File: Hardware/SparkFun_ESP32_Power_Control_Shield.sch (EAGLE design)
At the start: 66 parts, among them IC1 OP-AMP, IC2 OP-AMP, J1 5.5x2.1mm Barrel, U1 MC33926, U2 MC33926, U3 MC33926, U4 LM317

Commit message: Added measurements for board size and version number
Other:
- note added: "VCC : 5-28VDC"
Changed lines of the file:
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@@
 GND - SLOW - 3 us
 3.3V - FAST - 1.45 us</text>
+<text x="149.86" y="157.48" size="1.778" layer="97">VCC : 5-28VDC</text>
+<text x="172.72" y="81.28" size="1.778" layer="97">VCC : 5-28VDC</text>
 </plain>
 <instances>

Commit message: Added external capacitor
External capacitor will be populated by end user if too much ripple is
present on power rail.
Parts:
- added C19: Ext., SparkFun-Capacitors:100UF-POLAR-RADIAL-2.5MM-25V-20%
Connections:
- net GND: now also C19.-
- net VCC: now also C19.+
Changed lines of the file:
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@@
 <part name="GND26" library="SparkFun-PowerSymbols" deviceset="GND" device=""/>
 <part name="GND29" library="SparkFun-PowerSymbols" deviceset="GND" device=""/>
+<part name="C19" library="SparkFun-Capacitors" deviceset="100UF-POLAR" device="-RADIAL-2.5MM-25V-20%" value="Ext."/>
 </parts>
 <sheets>
@@
 <instance part="GND26" gate="1" x="203.2" y="40.64"/>
 <instance part="GND29" gate="1" x="233.68" y="40.64"/>
+<instance part="C19" gate="G$1" x="180.34" y="162.56" rot="MR0"/>
 </instances>
 <busses>
@@
 <wire x1="198.12" y1="172.72" x2="193.04" y2="172.72" width="0.1524" layer="91"/>
 <wire x1="193.04" y1="172.72" x2="187.96" y2="172.72" width="0.1524" layer="91"/>
-<wire x1="187.96" y1="172.72" x2="167.64" y2="172.72" width="0.1524" layer="91"/>
+<wire x1="187.96" y1="172.72" x2="180.34" y2="172.72" width="0.1524" layer="91"/>
+<wire x1="180.34" y1="172.72" x2="167.64" y2="172.72" width="0.1524" layer="91"/>
 <wire x1="198.12" y1="165.1" x2="198.12" y2="172.72" width="0.1524" layer="91"/>
 <junction x="198.12" y="172.72"/>
@@
 <wire x1="193.04" y1="175.26" x2="193.04" y2="172.72" width="0.1524" layer="91"/>
 <junction x="193.04" y="172.72"/>
+<pinref part="C19" gate="G$1" pin="+"/>
+<wire x1="180.34" y1="165.1" x2="180.34" y2="172.72" width="0.1524" layer="91"/>
+<junction x="180.34" y="172.72"/>
 </segment>
 <segment>
@@
 <wire x1="170.18" y1="167.64" x2="170.18" y2="142.24" width="0.1524" layer="91"/>
 <junction x="170.18" y="167.64"/>
-<wire x1="187.96" y1="142.24" x2="170.18" y2="142.24" width="0.1524" layer="91"/>
+<wire x1="187.96" y1="142.24" x2="180.34" y2="142.24" width="0.1524" layer="91"/>
 <pinref part="C15" gate="G$1" pin="2"/>
+<wire x1="180.34" y1="142.24" x2="170.18" y2="142.24" width="0.1524" layer="91"/>
 <wire x1="187.96" y1="142.24" x2="187.96" y2="157.48" width="0.1524" layer="91"/>
 <pinref part="C16" gate="G$1" pin="2"/>
@@
 <wire x1="238.76" y1="142.24" x2="228.6" y2="142.24" width="0.1524" layer="91"/>
 <junction x="228.6" y="142.24"/>
-</segment>
-<segment>
+<pinref part="C19" gate="G$1" pin="-"/>
+<wire x1="180.34" y1="157.48" x2="180.34" y2="142.24" width="0.1524" layer="91"/>
+<junction x="180.34" y="142.24"/>
+</segment>
+<segment>

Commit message: Proto design review changes
- Replaced SMD barrel jack with PTH
- Replaced op-amp resistor with 15k resistor
- Moved IO away from pins 34-39
- Attached disable input pin to IO pin
- Replaced 3/4 2-pin screw terminals with 6-pin screw terminal
- Added labeling to all IO pins used
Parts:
- C15: value 10uF -> Ext.; device SparkFun-Capacitors:10UF-1210-50V-20% -> SparkFun-Capacitors:100UF-POLAR-RADIAL-2.5MM-25V-20%
- C16, C18: value 0.1uF -> 10uF; device SparkFun-Capacitors:0.1UF-0603-100V-10% -> SparkFun-Capacitors:10UF-1210-50V-20%
- C17: value 10uF -> 0.1uF; device SparkFun-Capacitors:10UF-1210-50V-20% -> SparkFun-Capacitors:0.1UF-0603-100V-10%
- C19: value Ext. -> 0.1uF; device SparkFun-Capacitors:100UF-POLAR-RADIAL-2.5MM-25V-20% -> SparkFun-Capacitors:0.1UF-0603-100V-10%
- R11: value 390 -> 15k; device SparkFun-Resistors:390OHM-0603-1/10W-1% -> SparkFun-Resistors:15KOHM-0603-1/10W-1%
- U1, U2, U3: device Power_Control_Adapter_Temp:MC33926 -> SparkFun_ESP32_Power_Control_Shield_Temp:MC33926
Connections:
- net 3.3V: now also IC1G3.P$V+, IC2G3.P$V+; no longer IC1A.V+, IC2A.V+
- net 5V: now also C19.1; no longer C17.1
- net FB2: now also IC1G2.OUT; no longer IC1B.OUT
- net FB4: now also IC1G1.OUT; no longer IC1A.OUT
- net FB6: now also IC2G1.OUT; no longer IC2A.OUT
- net GND: now also C15.-, C19.2, IC1G3.P$V-, IC2G3.P$V-; no longer C15.2, C19.-, IC1A.V-, IC2A.V-
- net I_SENSE1: now also IC1G2.+IN; no longer IC1B.+IN
- net I_SENSE2: now also IC1G1.+IN; no longer IC1A.+IN
- net I_SENSE3: now also IC2G1.+IN; no longer IC2A.+IN
- net N$2: now also IC1G2.-IN; no longer IC1B.-IN
- net N$4: now also IC2G1.-IN; no longer IC2A.-IN
- net N$5: now also IC1G1.-IN; no longer IC1A.-IN
- net VCC: now also C15.+, C17.1; no longer C15.1, C19.+
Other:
- moved on the sheet: C10, C11, C12, C13, C14, C16, C17, C18, R10, R11, R12, R4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

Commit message: Same changes as design review
Forgot to save changes before commit.
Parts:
- removed J3, J4, J5: (no value), SparkFun-Connectors:CONN_023.5MM_LOCK
- added J6: (no value), SparkFun-Connectors:CONN_063.5MM-6
- J1: value 5.5x2.1mm Barrel -> POWER_JACKPTH_LOCK; device SparkFun-Connectors:POWER_JACKSMD -> SparkFun-Connectors:POWER_JACKPTH_LOCK
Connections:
- new net D1: B1.5, U1.D1, U2.D1, U3.D1
- net CTRL_2: now also B1.18; no longer B1.35
- net CTRL_3: now also B1.23; no longer B1.34
- net CTRL_6: now also B1.19; no longer B1.39
- net GND: no longer U1.D1, U2.D1, U3.D1
- net P_OUT1: now also J6.6; no longer J3.2
- net P_OUT2: now also J6.5; no longer J3.1
- net P_OUT3: now also J6.4; no longer J4.2
- net P_OUT4: now also J6.3; no longer J4.1
- net P_OUT5: now also J6.2; no longer J5.2
- net P_OUT6: now also J6.1; no longer J5.1

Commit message: QC Fixes
Replaced 0.1uF capacitors CAP-00810 with CAP-08390
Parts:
- C13, C14: device SparkFun-Capacitors:0.1UF-0603-25V-(+80/-20%) -> SparkFun-Capacitors:0.1UF-0603-100V-10%
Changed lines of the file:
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@@
 <part name="R10" library="SparkFun-Resistors" deviceset="15KOHM" device="-0603-1/10W-1%" value="15k"/>
 <part name="GND16" library="SparkFun-PowerSymbols" deviceset="GND" device=""/>
-<part name="C13" library="SparkFun-Capacitors" deviceset="0.1UF" device="-0603-25V-(+80/-20%)" value="0.1uF"/>
+<part name="C13" library="SparkFun-Capacitors" deviceset="0.1UF" device="-0603-100V-10%" value="0.1uF"/>
 <part name="SUPPLY13" library="SparkFun-PowerSymbols" deviceset="3.3V" device=""/>
 <part name="GND19" library="SparkFun-PowerSymbols" deviceset="GND" device=""/>
@@
 <part name="R12" library="SparkFun-Resistors" deviceset="15KOHM" device="-0603-1/10W-1%" value="15k"/>
 <part name="GND12" library="SparkFun-PowerSymbols" deviceset="GND" device=""/>
-<part name="C14" library="SparkFun-Capacitors" deviceset="0.1UF" device="-0603-25V-(+80/-20%)" value="0.1uF"/>
+<part name="C14" library="SparkFun-Capacitors" deviceset="0.1UF" device="-0603-100V-10%" value="0.1uF"/>
 <part name="SUPPLY14" library="SparkFun-PowerSymbols" deviceset="3.3V" device=""/>
 <part name="GND20" library="SparkFun-PowerSymbols" deviceset="GND" device=""/>

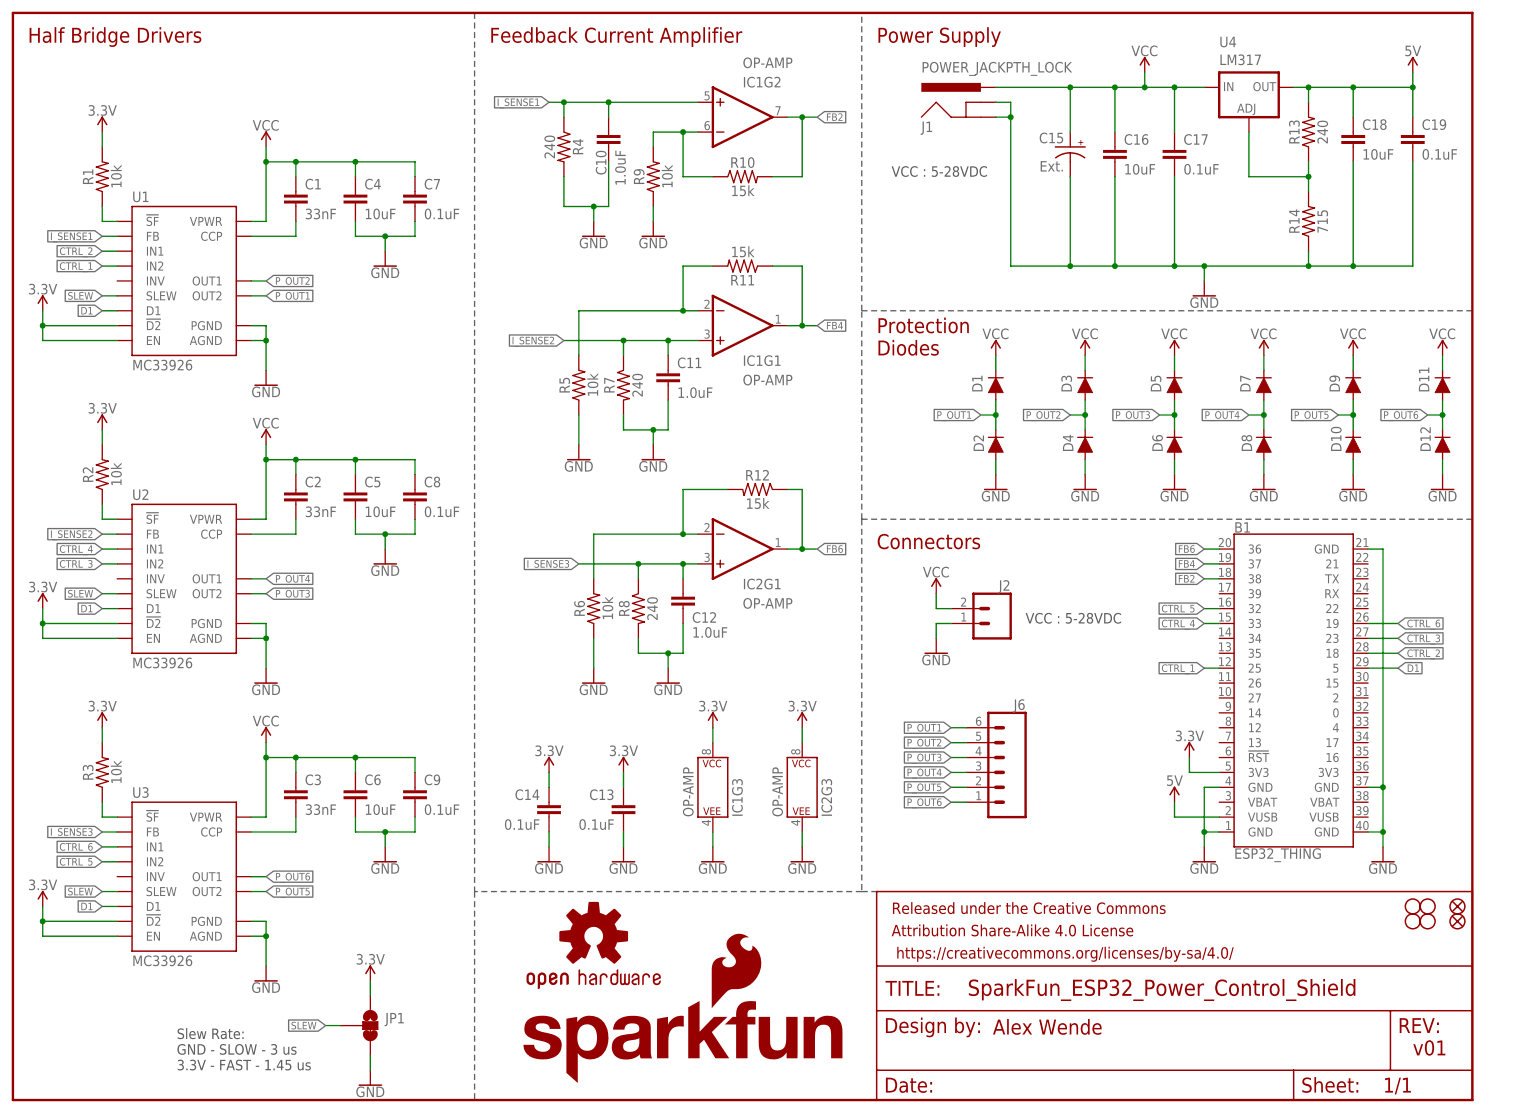
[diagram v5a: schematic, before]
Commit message: v10 Changes
- Flipped connectors from top layer to bottom
- Replaced 2-pin power connector with a 3-pin. Additional pin breaks out
5V power rail for a 5VDC fan.
- Added pull-down resistor to disable output (enabled by default).
- Replaced 5V LDO with DC/DC converter
- Replaced 240ohm resistors with 220ohm
- Replaced 15k feedback resistors with solder jumper and unpopulated PTH
resistor
- Increased trace width on VCC rail
- Added 5V bypass jumper to bypass the DC/DC converter which has a
minimum input voltage of 7V.
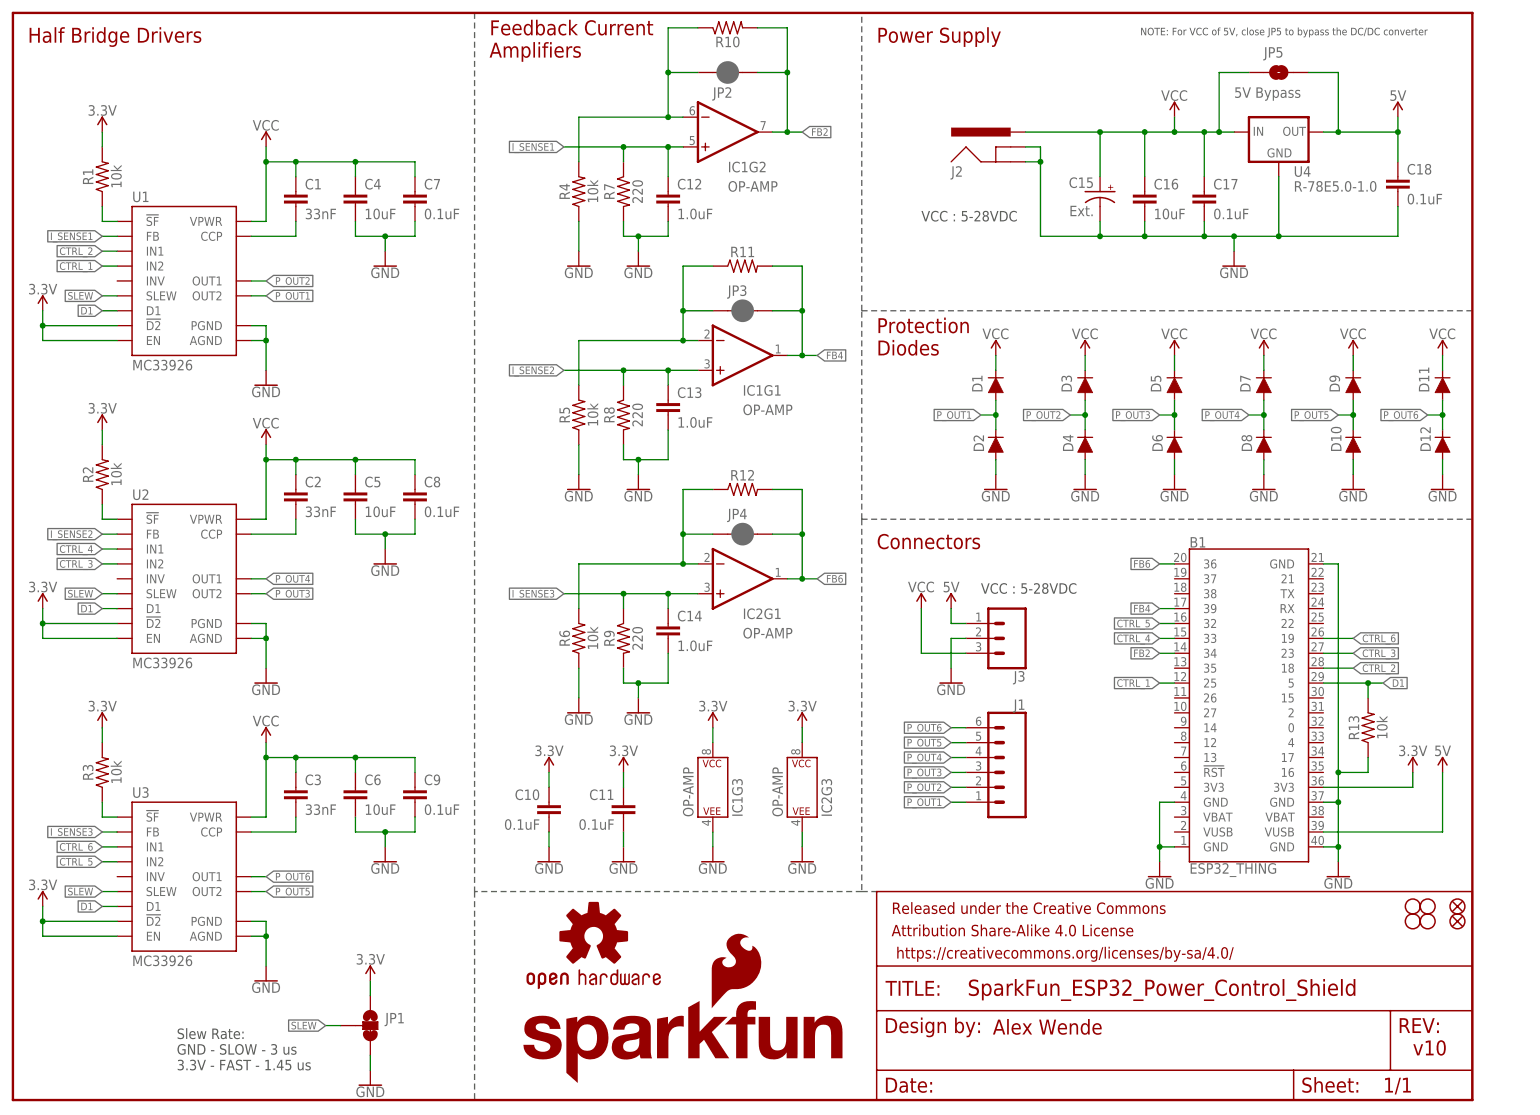
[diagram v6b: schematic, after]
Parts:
- removed C19: 0.1uF, SparkFun-Capacitors:0.1UF-0603-100V-10%
- removed J6: (no value), SparkFun-Connectors:CONN_063.5MM-6
- removed R14: 715, SparkFun-Resistors:715OHM-0603-1/10W-1%
- added J3: (no value), SparkFun-Connectors:CONN_03SCREW
- added JP2, JP3, JP4: JUMPER-SMT_2_NC_PASTE_NO-SILK, SparkFun-Jumpers:JUMPER-SMT_2_NC_PASTE_NO-SILK
- added JP5: 5V Bypass, SparkFun-Jumpers:JUMPER-SMT_2_NO_SILK
- C10, C11: value 1.0uF -> 0.1uF; device SparkFun-Capacitors:1.0UF-0603-16V-10% -> SparkFun-Capacitors:0.1UF-0603-100V-10%
- C13, C14: value 0.1uF -> 1.0uF; device SparkFun-Capacitors:0.1UF-0603-100V-10% -> SparkFun-Capacitors:1.0UF-0603-16V-10%
- C18: value 10uF -> 0.1uF; device SparkFun-Capacitors:10UF-1210-50V-20% -> SparkFun-Capacitors:0.1UF-0603-100V-10%
- J1: value POWER_JACKPTH_LOCK -> (none); device SparkFun-Connectors:POWER_JACKPTH_LOCK -> SparkFun-Connectors:CONN_063.5MM-6
- J2: value (none) -> POWER_JACKPTH_LOCK; device SparkFun-Connectors:CONN_023.5MM_LOCK -> SparkFun-Connectors:POWER_JACKPTH_LOCK
- R10, R11, R12: value 15k -> 1KOHM-HORIZ-1/4W-1%; device SparkFun-Resistors:15KOHM-0603-1/10W-1% -> SparkFun-Resistors:1KOHM-HORIZ-1/4W-1%
- R13, R4: value 240 -> 10k; device SparkFun-Resistors:240OHM-0603-1/10W-1% -> SparkFun-Resistors:10KOHM-0603-1/10W-1%
- R7, R8: value 240 -> 220; device SparkFun-Resistors:240OHM-0603-1/10W-1% -> SparkFun-Resistors:220OHM-0603-1/10W-1%
- R9: value 10k -> 220; device SparkFun-Resistors:10KOHM-0603-1/10W-1% -> SparkFun-Resistors:220OHM-0603-1/10W-1%
- U4: value LM317 -> R-78E5.0-1.0; device SparkFun-IC-Power:V_REG_317DPACK -> SparkFun-IC-Power:R-78E5.0-1.0
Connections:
- removed net ADJ: R13.1, R14.2, U4.ADJ
- net 3.3V: now also B1.3V3@36, C10.1, C11.1; no longer B1.3V3@5, C13.1, C14.1
- net 5V: now also B1.VUSB@39, J3.1, JP5.2; no longer B1.VUSB@2, C19.1, R13.2
- net D1: now also R13.2
- net FB2: now also B1.34, JP2.2; no longer B1.38
- net FB4: now also B1.39, JP3.2, R11.2; no longer B1.37, R11.1
- net FB6: now also JP4.2, R12.2; no longer R12.1
- net GND: now also J2.GND, J2.GNDBREAK, J3.2, R13.1, R4.1, R9.2, U4.GND; no longer C19.2, J1.GND, J1.GNDBREAK, J2.1, R14.1, R4.2, R9.1
- net I_SENSE1: now also C12.1, R7.1; no longer C10.1, R4.1
- net I_SENSE2: now also C13.1, R8.1; no longer C11.1, R7.1
- net I_SENSE3: now also C14.1, R9.1; no longer C12.1, R8.1
- net N$2: now also JP2.1, R4.2; no longer R9.2
- net N$4: now also JP4.1, R12.1; no longer R12.2
- net N$5: now also JP3.1, R11.1; no longer R11.2
- net P_OUT1: now also J1.1; no longer J6.6
- net P_OUT2: now also J1.2; no longer J6.5
- net P_OUT3: now also J1.3; no longer J6.4
- net P_OUT4: now also J1.4; no longer J6.3
- net P_OUT5: now also J1.5; no longer J6.2
- net P_OUT6: now also J1.6; no longer J6.1
- net VCC: now also J2.PWR, J3.3, JP5.1; no longer J1.PWR, J2.2
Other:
- note added: "Feedback Current Amplifiers"
- note added: "NOTE: For VCC of 5V, close JP5 to bypass the DC/DC converter"
- note added: "v10"
- note removed: "Feedback Current Amplifier"
- note removed: "v01"
- moved on the sheet: B1, C10, C11, C12, C13, C14, C15, C16, C17, C18, IC1G1, IC1G2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

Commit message: v10 changes additional
minor schematic layout changes, added values for the op-amps and diodes.
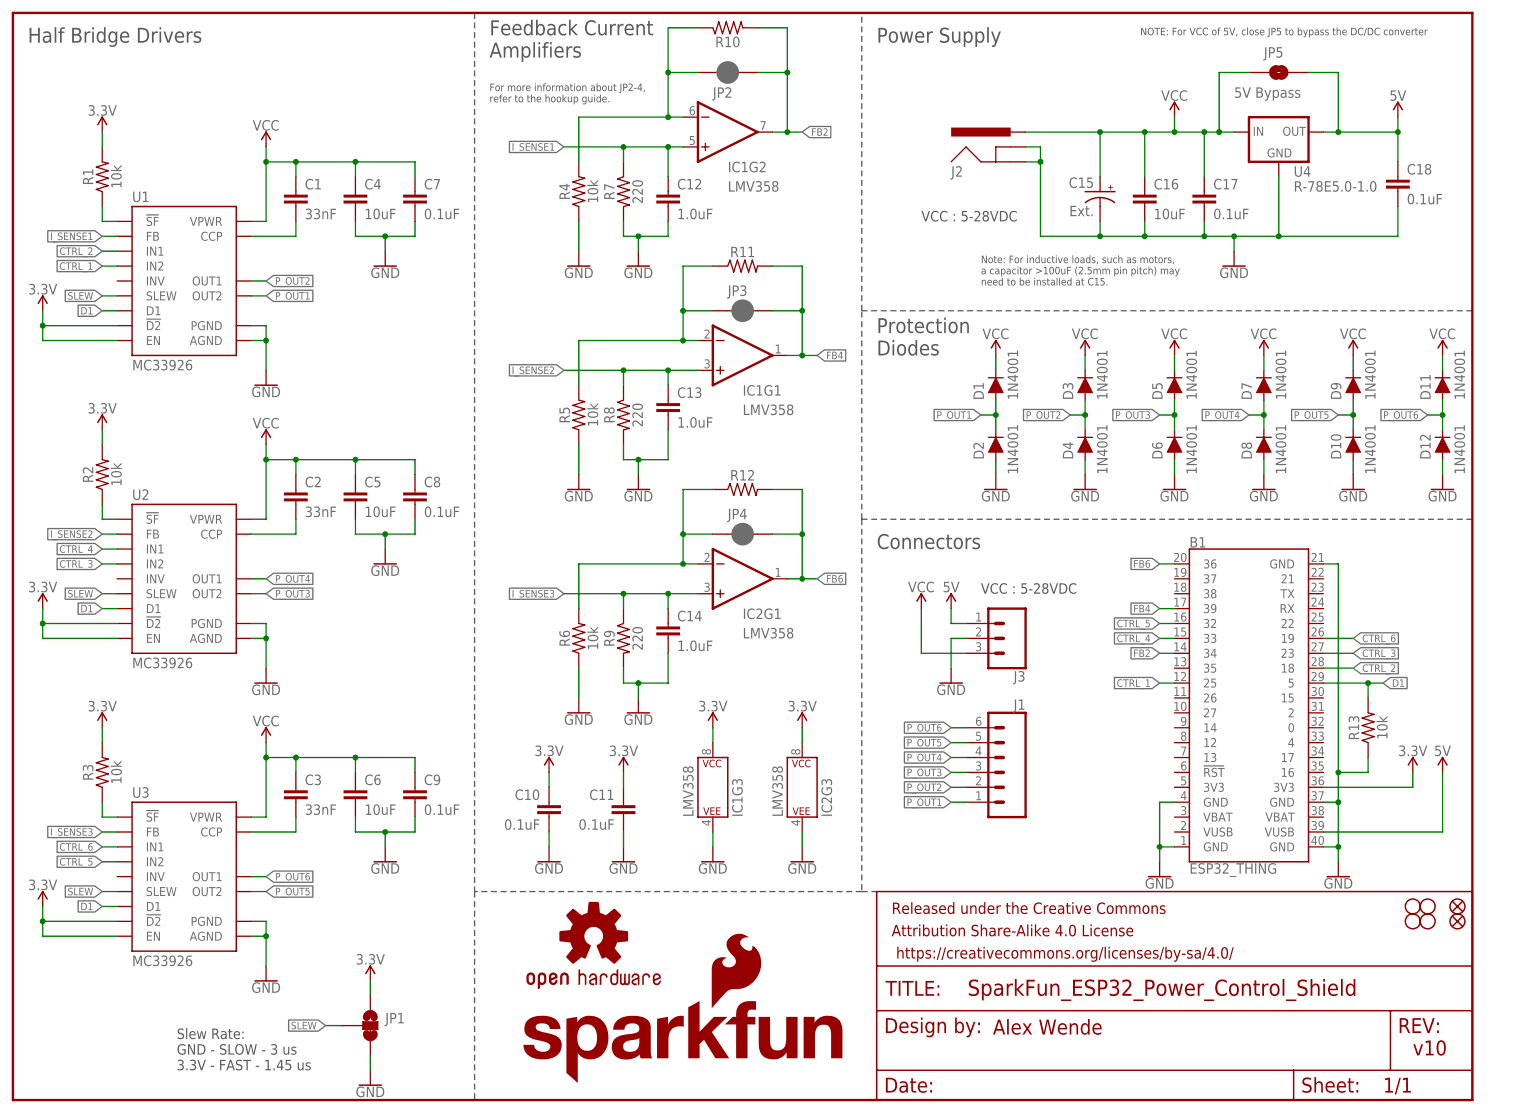
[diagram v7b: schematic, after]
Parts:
- D1, D10, D11, D12, D2, D3, D4, D5, D6, D7, D8, D9: value 1A/50V/1.1V -> 1N4001
- IC1, IC2: value OP-AMP -> LMV358
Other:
- note added: "For more information about JP2-4, refer to the hookup guide."
- note added: "Note: For inductive loads, such as motors, a capacitor >100uF (2.5mm pin pitch) may need to be installed at C15."
